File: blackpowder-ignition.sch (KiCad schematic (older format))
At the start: 6 parts, among them J8 Conn_01x02, U1 TCA9555PWR

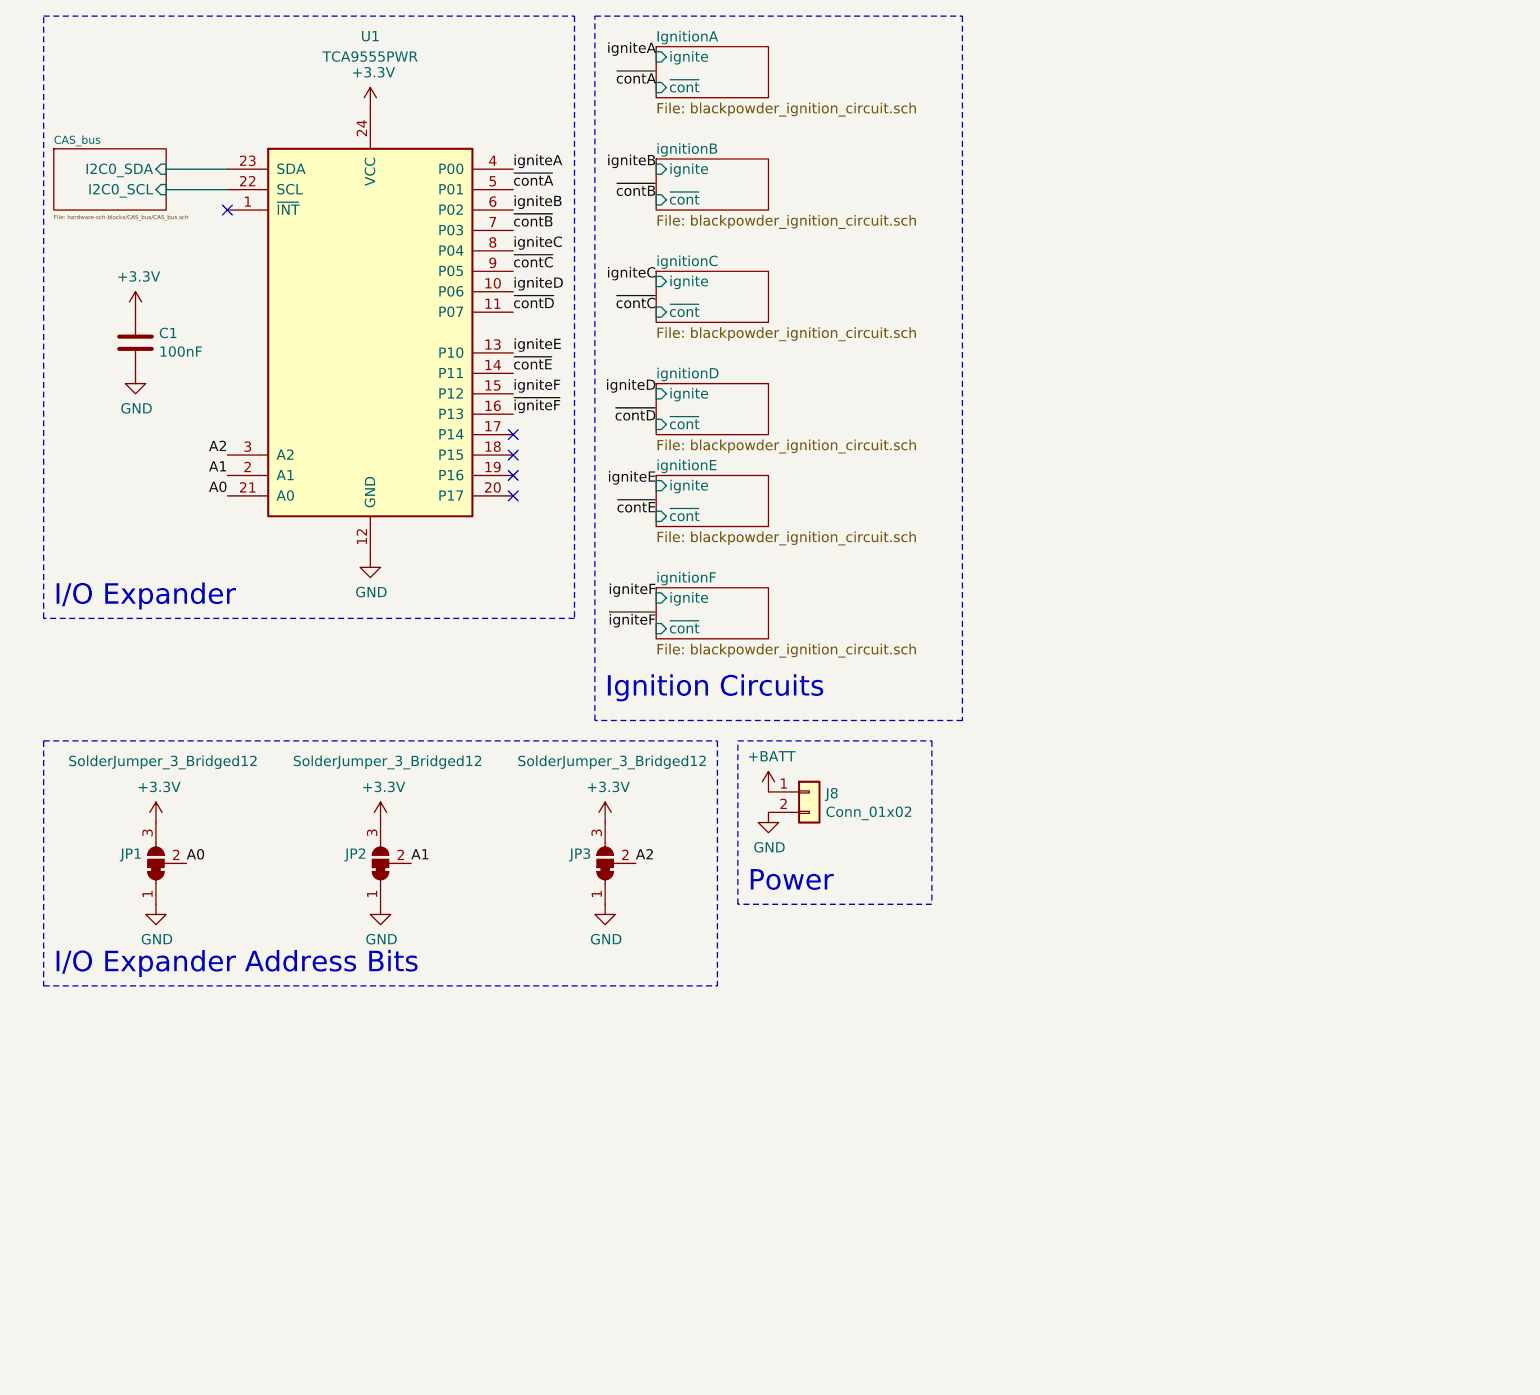
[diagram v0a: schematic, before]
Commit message: removed circuits that can't be fit in
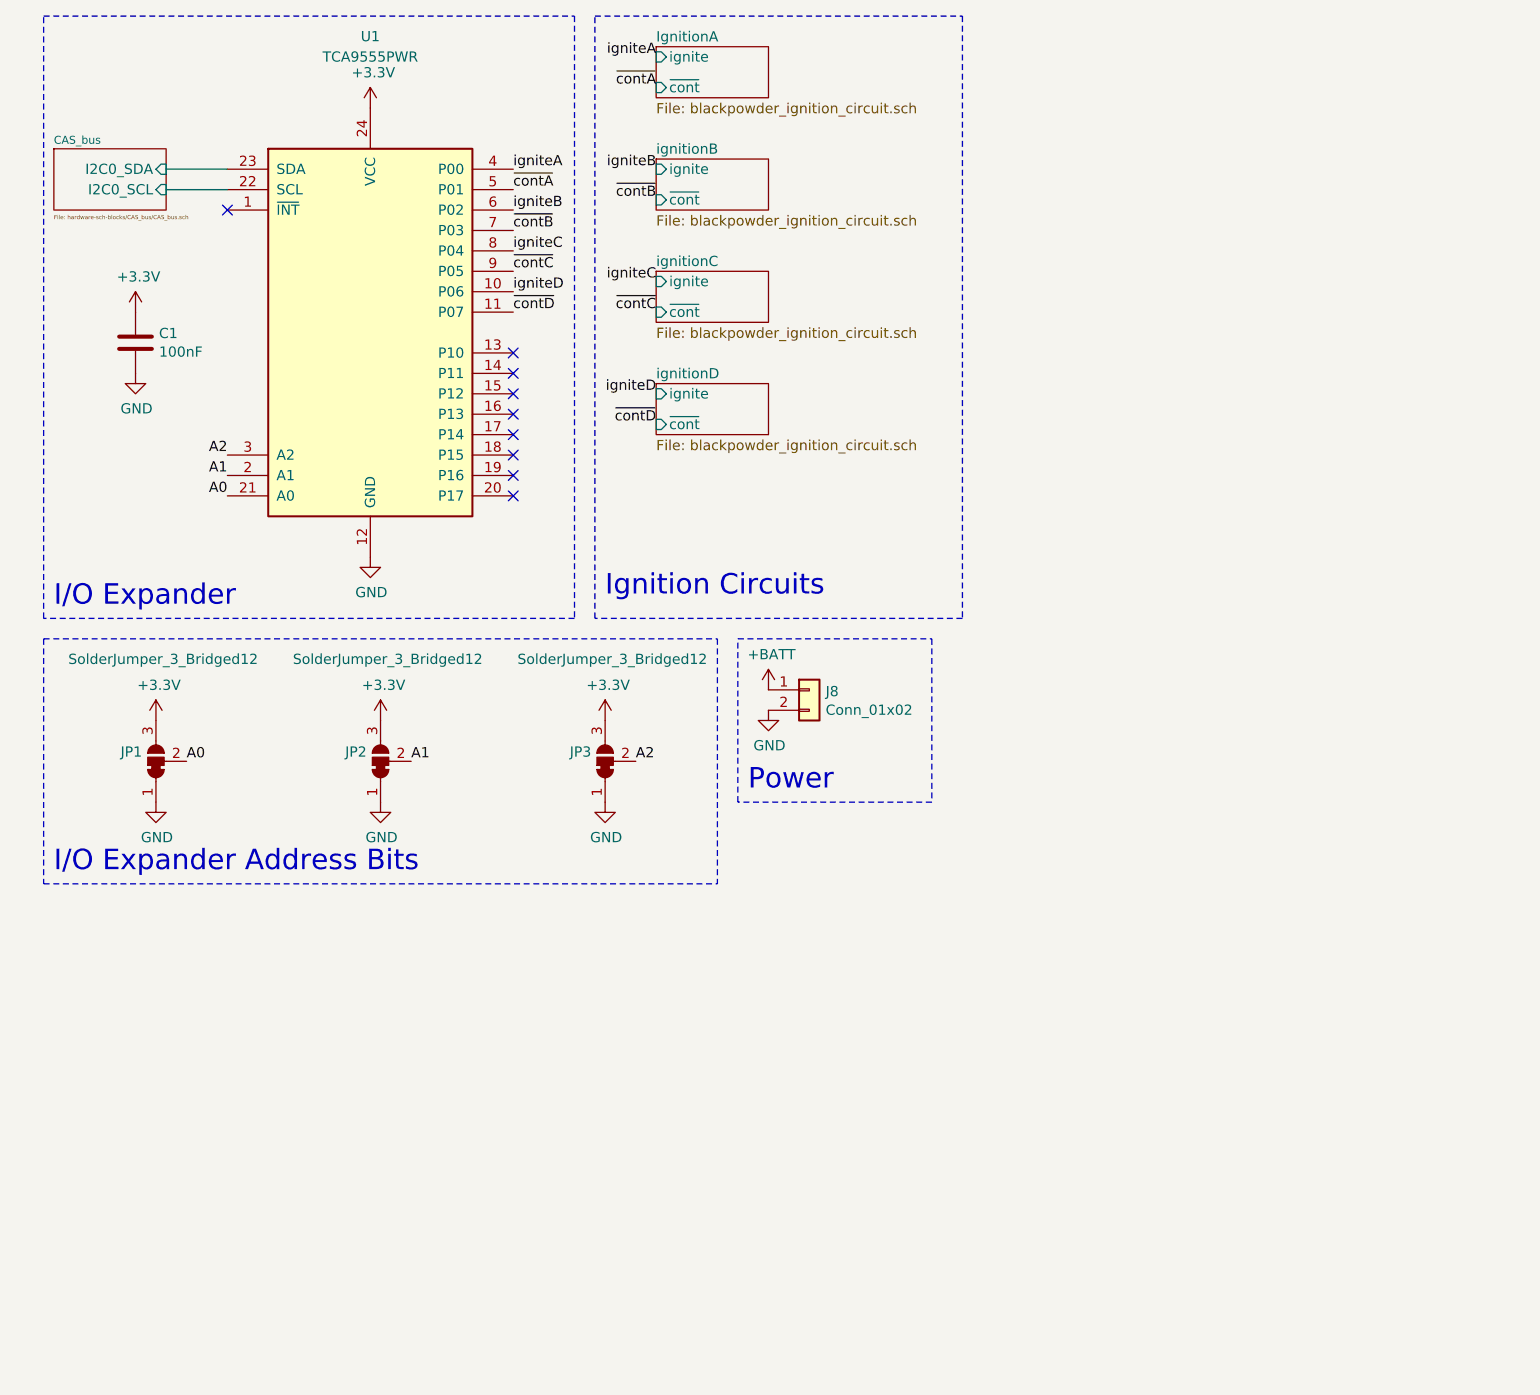
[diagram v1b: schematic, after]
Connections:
- net igniteE: no longer names the net of U1.13 (P10)
- net igniteF: no longer names the net of U1.15 (P12)
- net ~contE~: no longer names the net of U1.14 (P11)
- net ~igniteF~: no longer names the net of U1.16 (P13)
- no-connect marks 5 -> 9
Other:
- moved on the sheet: J8, JP1, JP2, JP3
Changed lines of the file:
@@
 $Descr A4 11693 8268
 encoding utf-8
-Sheet 1 8
+Sheet 1 6
 Title ""
 Date ""
@@
 $EndSheet
 $Sheet
-S 3550 2800 550  250
-U 5EB223E6
-F0 "ignitionE" 50
-F1 "blackpowder_ignition_circuit.sch" 50
-F2 "ignite" I L 3550 2850 50
-F3 "~cont~" I L 3550 3000 50
-$EndSheet
-$Sheet
-S 3550 3350 550  250
-U 5EB223EA
-F0 "ignitionF" 50
-F1 "blackpowder_ignition_circuit.sch" 50
-F2 "ignite" I L 3550 3400 50
-F3 "~cont~" I L 3550 3550 50
-$EndSheet
-$Sheet
 S 600  1200 550  300
 U 5ED2D9A2
@@
 L Jumper:SolderJumper_3_Bridged12 JP3
 U 1 1 5ED6038D
-P 3300 4700
-F 0 "JP3" V 3346 4768 50  0000 L CNN
-F 1 "SolderJumper_3_Bridged12" V 3800 4200 50  0000 L CNN
-F 2 "Jumper:SolderJumper-3_P1.3mm_Bridged12_RoundedPad1.0x1.5mm" H 3300 4700 50  0001 C CNN
-F 3 "~" H 3300 4700 50  0001 C CNN
-	1    3300 4700
+P 3300 4200
+F 0 "JP3" V 3346 4268 50  0000 L CNN
+F 1 "SolderJumper_3_Bridged12" V 3800 3700 50  0000 L CNN
+F 2 "Jumper:SolderJumper-3_P1.3mm_Bridged12_RoundedPad1.0x1.5mm" H 3300 4200 50  0001 C CNN
+F 3 "~" H 3300 4200 50  0001 C CNN
+	1    3300 4200
 	0    -1   -1   0
 $EndComp
@@
 L power:+3.3V #PWR0139
 U 1 1 5ED64CA6
-P 3300 4500
-F 0 "#PWR0139" H 3300 4350 50  0001 C CNN
-F 1 "+3.3V" H 3315 4673 50  0000 C CNN
-F 2 "" H 3300 4500 50  0001 C CNN
-F 3 "" H 3300 4500 50  0001 C CNN
-	1    3300 4500
+P 3300 4000
+F 0 "#PWR0139" H 3300 3850 50  0001 C CNN
+F 1 "+3.3V" H 3315 4173 50  0000 C CNN
+F 2 "" H 3300 4000 50  0001 C CNN
+F 3 "" H 3300 4000 50  0001 C CNN
+	1    3300 4000
 	1    0    0    -1
 $EndComp
@@
 L power:GND #PWR0140
 U 1 1 5ED6509D
-P 3300 4900
-F 0 "#PWR0140" H 3300 4650 50  0001 C CNN
-F 1 "GND" H 3305 4727 50  0000 C CNN
-F 2 "" H 3300 4900 50  0001 C CNN
-F 3 "" H 3300 4900 50  0001 C CNN
-	1    3300 4900
+P 3300 4400
+F 0 "#PWR0140" H 3300 4150 50  0001 C CNN
+F 1 "GND" H 3305 4227 50  0000 C CNN
+F 2 "" H 3300 4400 50  0001 C CNN
+F 3 "" H 3300 4400 50  0001 C CNN
+	1    3300 4400
 	1    0    0    -1
 $EndComp
@@
 L Jumper:SolderJumper_3_Bridged12 JP2
 U 1 1 5ED672FE
-P 2200 4700
-F 0 "JP2" V 2246 4768 50  0000 L CNN
-F 1 "SolderJumper_3_Bridged12" V 2700 4200 50  0000 L CNN
-F 2 "Jumper:SolderJumper-3_P1.3mm_Bridged12_RoundedPad1.0x1.5mm" H 2200 4700 50  0001 C CNN
-F 3 "~" H 2200 4700 50  0001 C CNN
-	1    2200 4700
+P 2200 4200
+F 0 "JP2" V 2246 4268 50  0000 L CNN
+F 1 "SolderJumper_3_Bridged12" V 2700 3700 50  0000 L CNN
+F 2 "Jumper:SolderJumper-3_P1.3mm_Bridged12_RoundedPad1.0x1.5mm" H 2200 4200 50  0001 C CNN
+F 3 "~" H 2200 4200 50  0001 C CNN
+	1    2200 4200
 	0    -1   -1   0
 $EndComp
@@
 L power:+3.3V #PWR0141
 U 1 1 5ED67304
-P 2200 4500
-F 0 "#PWR0141" H 2200 4350 50  0001 C CNN
-F 1 "+3.3V" H 2215 4673 50  0000 C CNN
-F 2 "" H 2200 4500 50  0001 C CNN
-F 3 "" H 2200 4500 50  0001 C CNN
-	1    2200 4500
+P 2200 4000
+F 0 "#PWR0141" H 2200 3850 50  0001 C CNN
+F 1 "+3.3V" H 2215 4173 50  0000 C CNN
+F 2 "" H 2200 4000 50  0001 C CNN
+F 3 "" H 2200 4000 50  0001 C CNN
+	1    2200 4000
 	1    0    0    -1
 $EndComp
@@
 L power:GND #PWR0142
 U 1 1 5ED6730A
-P 2200 4900
-F 0 "#PWR0142" H 2200 4650 50  0001 C CNN
-F 1 "GND" H 2205 4727 50  0000 C CNN
-F 2 "" H 2200 4900 50  0001 C CNN
-F 3 "" H 2200 4900 50  0001 C CNN
-	1    2200 4900
+P 2200 4400
+F 0 "#PWR0142" H 2200 4150 50  0001 C CNN
+F 1 "GND" H 2205 4227 50  0000 C CNN
+F 2 "" H 2200 4400 50  0001 C CNN
+F 3 "" H 2200 4400 50  0001 C CNN
+	1    2200 4400
 	1    0    0    -1
 $EndComp
@@
 L Jumper:SolderJumper_3_Bridged12 JP1
 U 1 1 5ED68598
-P 1100 4700
-F 0 "JP1" V 1146 4768 50  0000 L CNN
-F 1 "SolderJumper_3_Bridged12" V 1600 4200 50  0000 L CNN
-F 2 "Jumper:SolderJumper-3_P1.3mm_Bridged12_RoundedPad1.0x1.5mm" H 1100 4700 50  0001 C CNN
-F 3 "~" H 1100 4700 50  0001 C CNN
-	1    1100 4700
+P 1100 4200
+F 0 "JP1" V 1146 4268 50  0000 L CNN
+F 1 "SolderJumper_3_Bridged12" V 1600 3700 50  0000 L CNN
+F 2 "Jumper:SolderJumper-3_P1.3mm_Bridged12_RoundedPad1.0x1.5mm" H 1100 4200 50  0001 C CNN
+F 3 "~" H 1100 4200 50  0001 C CNN
+	1    1100 4200
 	0    -1   -1   0
 $EndComp
@@
 L power:+3.3V #PWR0143
 U 1 1 5ED6859E
-P 1100 4500
-F 0 "#PWR0143" H 1100 4350 50  0001 C CNN
-F 1 "+3.3V" H 1115 4673 50  0000 C CNN
-F 2 "" H 1100 4500 50  0001 C CNN
-F 3 "" H 1100 4500 50  0001 C CNN
-	1    1100 4500
+P 1100 4000
+F 0 "#PWR0143" H 1100 3850 50  0001 C CNN
+F 1 "+3.3V" H 1115 4173 50  0000 C CNN
+F 2 "" H 1100 4000 50  0001 C CNN
+F 3 "" H 1100 4000 50  0001 C CNN
+	1    1100 4000
 	1    0    0    -1
 $EndComp
@@
 L power:GND #PWR0144
 U 1 1 5ED685A4
-P 1100 4900
-F 0 "#PWR0144" H 1100 4650 50  0001 C CNN
-F 1 "GND" H 1105 4727 50  0000 C CNN
-F 2 "" H 1100 4900 50  0001 C CNN
-F 3 "" H 1100 4900 50  0001 C CNN
-	1    1100 4900
+P 1100 4400
+F 0 "#PWR0144" H 1100 4150 50  0001 C CNN
+F 1 "GND" H 1105 4227 50  0000 C CNN
+F 2 "" H 1100 4400 50  0001 C CNN
+F 3 "" H 1100 4400 50  0001 C CNN
+	1    1100 4400
 	1    0    0    -1
 $EndComp
@@
 L Connector_Generic:Conn_01x02 J8
 U 1 1 5ED34396
-P 4300 4350
-F 0 "J8" H 4380 4342 50  0000 L CNN
-F 1 "Conn_01x02" H 4380 4251 50  0000 L CNN
-F 2 "Connector_Molex:Molex_Mini-Fit_Jr_5569-02A2_2x01_P4.20mm_Horizontal" H 4300 4350 50  0001 C CNN
-F 3 "~" H 4300 4350 50  0001 C CNN
-	1    4300 4350
+P 4300 3850
+F 0 "J8" H 4380 3842 50  0000 L CNN
+F 1 "Conn_01x02" H 4380 3751 50  0000 L CNN
+F 2 "Connector_Molex:Molex_Mini-Fit_Jr_5569-02A2_2x01_P4.20mm_Horizontal" H 4300 3850 50  0001 C CNN
+F 3 "~" H 4300 3850 50  0001 C CNN
+	1    4300 3850
 	1    0    0    -1
 $EndComp
@@
 L power:+BATT #PWR01
 U 1 1 5ED35440
-P 4100 4350
-F 0 "#PWR01" H 4100 4200 50  0001 C CNN
-F 1 "+BATT" H 4115 4523 50  0000 C CNN
-F 2 "" H 4100 4350 50  0001 C CNN
-F 3 "" H 4100 4350 50  0001 C CNN
-	1    4100 4350
+P 4100 3850
+F 0 "#PWR01" H 4100 3700 50  0001 C CNN
+F 1 "+BATT" H 4115 4023 50  0000 C CNN
+F 2 "" H 4100 3850 50  0001 C CNN
+F 3 "" H 4100 3850 50  0001 C CNN
+	1    4100 3850
 	1    0    0    -1
 $EndComp
@@
 L power:GND #PWR02
 U 1 1 5ED356CF
-P 4100 4450
-F 0 "#PWR02" H 4100 4200 50  0001 C CNN
-F 1 "GND" H 4105 4277 50  0000 C CNN
-F 2 "" H 4100 4450 50  0001 C CNN
-F 3 "" H 4100 4450 50  0001 C CNN
-	1    4100 4450
+P 4100 3950
+F 0 "#PWR02" H 4100 3700 50  0001 C CNN
+F 1 "GND" H 4105 3777 50  0000 C CNN
+F 2 "" H 4100 3950 50  0001 C CNN
+F 3 "" H 4100 3950 50  0001 C CNN
+	1    4100 3950
 	1    0    0    -1
 $EndComp
@@
 Text Label 2850 2000 0    50   ~ 0
 ~contD~
-Text Label 2850 2200 0    50   ~ 0
-igniteE
-Text Label 2850 2300 0    50   ~ 0
-~contE~
-Text Label 2850 2400 0    50   ~ 0
-igniteF
-Text Label 2850 2500 0    50   ~ 0
-~igniteF~
 Text Label 3550 900  2    50   ~ 0
 ~contA~
@@
 Text Label 3550 2550 2    50   ~ 0
 ~contD~
-Text Label 3550 2850 2    50   ~ 0
-igniteE
-Text Label 3550 3000 2    50   ~ 0
-~contE~
-Text Label 3550 3400 2    50   ~ 0
-igniteF
-Text Label 3550 3550 2    50   ~ 0
-~igniteF~
 Text Label 1450 2900 2    50   ~ 0
 A0
@@
 Text Label 1450 2700 2    50   ~ 0
 A2
-Text Label 1250 4700 0    50   ~ 0
+Text Label 1250 4200 0    50   ~ 0
 A0
-Text Label 2350 4700 0    50   ~ 0
+Text Label 2350 4200 0    50   ~ 0
 A1
-Text Label 3450 4700 0    50   ~ 0
+Text Label 3450 4200 0    50   ~ 0
 A2
 Wire Notes Line
@@
 Text Notes 600  3450 0    100  ~ 0
 I/O Expander
-Text Notes 600  5250 0    100  ~ 0
+Text Notes 600  4750 0    100  ~ 0
 I/O Expander Address Bits
 Wire Notes Line
-	550  4100 550  5300
-Text Notes 3300 3900 0    100  ~ 0
+	550  3600 550  4800
+Text Notes 3300 3400 0    100  ~ 0
 Ignition Circuits
 Wire Notes Line
 	3250 550  5050 550
-Wire Notes Line
-	5050 550  5050 4000
-Wire Notes Line
-	5050 4000 3250 4000
-Wire Notes Line
-	3250 4000 3250 550
-Text Notes 4000 4850 0    100  ~ 0
+Text Notes 4000 4350 0    100  ~ 0
 Power
 Wire Notes Line
-	3950 4100 4900 4100
-Wire Notes Line
-	4900 4100 4900 4900
-Wire Notes Line
-	4900 4900 3950 4900
-Wire Notes Line
-	3950 4900 3950 4100
-Wire Notes Line
-	3850 4100 3850 5300
-Wire Notes Line
-	550  4100 3850 4100
-Wire Notes Line
-	550  5300 3850 5300
+	3950 3600 4900 3600
+Wire Notes Line
+	4900 3600 4900 4400
+Wire Notes Line
+	4900 4400 3950 4400
+Wire Notes Line
+	3950 4400 3950 3600
+Wire Notes Line
+	3850 3600 3850 4800
+Wire Notes Line
+	550  3600 3850 3600
+Wire Notes Line
+	550  4800 3850 4800
+NoConn ~ 2850 2400
+NoConn ~ 2850 2500
+Wire Notes Line
+	5050 550  5050 3500
+Wire Notes Line
+	5050 3500 3250 3500
+Wire Notes Line
+	3250 3500 3250 550
+NoConn ~ 2850 2200
+NoConn ~ 2850 2300
 $EndSCHEMATC
